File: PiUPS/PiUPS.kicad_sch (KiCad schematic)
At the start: 101 parts, among them J1 USB_C_Receptacle_USB2.0, J2 Raspberry_Pi_2_3, J3 USB_A, J4 USB_B_Micro, J5 Screw_Terminal_01x02, J6 Screw_Terminal_01x02, Q1 IRF7404, Q2 IRF7404, Q3 IRLML2803TRPBF, Q4 IRF7404, Q5 IRF7404, Q6 IRLML2803TRPBF, Q7 IRLML2803TRPBF, SW1 MODE (JS102011SAQN), SW2 SW_MEC_5E, U1 LM393, U2 BQ25601, U3 TPS61088RHLR, U4 DS3231M

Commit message: minor improvements and cleanup
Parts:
- removed R17: USR, Resistor_SMD:R_0805_2012Metric_Pad1.20x1.40mm_HandSolder, symbol Device:R
- added R?: 470, Resistor_SMD:R_0805_2012Metric_Pad1.20x1.40mm_HandSolder, symbol Device:R
- R?: value 100 -> 470
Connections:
- net +BATT: now also SW2.1, SW2.2
- net GND: no longer SW2.1, SW2.2
- net at SW2.3 (K), SW2.4 (A): now also R?.2; no longer U2.12 (~{QON})
- net at Q?.1, R?.1, R?.2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: now also R?.1
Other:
- note added: "100 works"
- note added: "Enable without input voltage"
- note added: "Raplce with bq25895"
- note removed: "Probably can be lowered to 470"
- moved on the sheet: D4, D?, SW2, U1C

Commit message: assigned footprints
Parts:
- removed C1: 47nF, Capacitor_SMD:C_0805_2012Metric_Pad1.18x1.45mm_HandSolder, symbol Device:C
- removed C15, C18: 10uF, Capacitor_SMD:C_1206_3216Metric_Pad1.33x1.80mm_HandSolder, symbol Device:C
- removed D2: LED_G, LED_SMD:LED_0805_2012Metric, symbol Device:LED
- removed R28, R31, R33: 10k, Resistor_SMD:R_0805_2012Metric_Pad1.20x1.40mm_HandSolder, symbol Device:R
- removed U2: BQ25601, Package_DFN_QFN:Texas_S-PWQFN-N24_EP2.7x2.7mm_ThermalVias, symbol Battery_Management:BQ25601
- added C10, C6: 10uF, Capacitor_SMD:C_1206_3216Metric_Pad1.33x1.80mm_HandSolder, symbol Device:C
- added C12: 100nF, Capacitor_SMD:C_0805_2012Metric_Pad1.18x1.45mm_HandSolder, symbol Device:C
- added C5: 47nF, Capacitor_SMD:C_0805_2012Metric_Pad1.18x1.45mm_HandSolder, symbol Device:C
- added D3, D4: 1PS76SB40.115, Diode_SMD:D_SOD-323_HandSoldering, symbol Diode:1N4007
- added R1, R17: 10k, Resistor_SMD:R_0805_2012Metric_Pad1.20x1.40mm_HandSolder, symbol Device:R
- added R11, R12, R24, R27: 470, Resistor_SMD:R_0805_2012Metric_Pad1.20x1.40mm_HandSolder, symbol Device:R
- added R19: 1k, Resistor_SMD:R_0805_2012Metric_Pad1.20x1.40mm_HandSolder, symbol Device:R
- added R23: 100, Resistor_SMD:R_0805_2012Metric_Pad1.20x1.40mm_HandSolder, symbol Device:R
- added RT1: 10k, Resistor_SMD:R_0603_1608Metric, symbol Device:R
- added U2: BQ25895RTW, Package_DFN_QFN:Texas_S-PWQFN-N24_EP2.7x2.7mm_ThermalVias, symbol Battery_Management:BQ25895RTW
- added U4: DW01, Package_TO_SOT_SMD:SOT-23-6, symbol dw01:DW01
- added U5: FS8205A, Package_SO:TSSOP-8_4.4x3mm_P0.65mm, symbol fs8205a:FS8205A
- C20: renamed from C21; value 220uF -> 1000uF
- D1: renamed from D?; value 1N4007 -> 1PS76SB40.115; footprint Diode_THT:D_DO-41_SOD81_P10.16mm_Horizontal -> Diode_SMD:D_SOD-323_HandSoldering
- D2: renamed from D3; footprint LED_SMD:LED_0805_2012Metric -> LED_SMD:LED_1206_3216Metric_Pad1.42x1.75mm_HandSolder
- D6: renamed from D4; value 1N4001 -> 1PS76SB40.115; footprint Diode_SMD:D_1206_3216Metric_Pad1.42x1.75mm_HandSolder -> Diode_SMD:D_SOD-323_HandSoldering
- J2: renamed from J4; footprint Connector_USB:USB_Micro-B_GCT_USB3076-30-A -> Connector_USB:USB_Micro-B_Amphenol_10103594-0001LF_Horizontal
- J4: renamed from J3; footprint Connector_USB:USB_A_Stewart_SS-52100-001_Horizontal -> USB:SAMTEC_USB-A-S-X-X-SM2
- R13: value 5.1k -> 10k
- gave numbers to parts that had none: 11
- renumbered C9 to C1, C16 to C11, C5 to C13, C12 to C14, C6 to C15, C14 to C16, C7 to C17, C17 to C18, C13 to C19, C4 to C2, C22 to C21, C23 to C22, C24 to C23, C25 to C24, C20 to C26, C10 to C3, C11 to C4, C19 to C7, C2 to C8, C3 to C9, D1 to D5, J6 to J3, J2 to J6, L2 to L1, L1 to L2, Q7 to Q3, Q1 to Q4, Q3 to Q5, Q4 to Q6, Q6 to Q7, Q2 to Q8, Q5 to Q9, R9 to R10, R25 to R16, R1 to R20, R5 to R21, R27 to R22, R24 to R25, R7 to R26, R20 to R28, R3 to R29, R16 to R30, R26 to R31, R2 to R32, R19 to R33, R21 to R34, R38 to R36, R39 to R37, R36 to R38, R4 to R39, R37 to R40, R23 to R41, R6 to R42, R12 to R43, R30 to R44, R14 to R45, R35 to R46, R10 to R47, R8 to R48, R34 to R49, R32 to R6, R11 to R7, R15 to R9, SW2 to SW1, SW1 to SW2, U4 to U6
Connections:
- net +5V: now also R24.2, U2.1 (VBUS)
- net +BATT: now also R23.1, U2.13 (BAT), U2.14 (BAT)
- net 2V4: now also R27.1
- net GND: now also C12.2, R1.1, U4.6 (GND), U5.2 (S1), U5.3 (S1); no longer C8.2, C9.2, R18.2
- net INT: now also U2.7 (INT)
- net SCL: now also U2.5 (SCL)
- net SDA: now also U2.6 (SDA)
- net VOUT: now also R26.2, R35.2, U1.8 (V+), R27.2; no longer SW2.2 (B)
- net VSYS: now also R9.1, U2.15 (SYS), U2.16 (SYS); no longer D2.2 (A)
- net at L2.1: now also C5.1, U2.19 (SW), U2.20 (SW)
- net at R9.2: now also D2.2 (A)
- net at R13.2: now also U2.9 (~{CE})
- net GND1: now reaches R18.1
- net GND1: now also C8.2, C9.2, R13.1, C10.2, C6.1, R12.2, R19.1, RT1.1, U2.17 (PGND), U2.18 (PGND), U2.25 (PGND), U2.8 (OTG), U5.6 (S2), U5.7 (S2)
- net at D2.1 (K): now also U2.4 (STAT); no longer R9.1
- net at SW2.3 (C): now also R1.2
- net at R2.1, R3.2, R4.2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: now also SW2.1 (A); no longer Q1.1
- new net: Q1.1, SW2.2 (B)
- new net: D4.1 (K), U4.1 (OD), U5.4 (G1)
- new net: R19.2, U4.2 (CS)
- new net: D3.1 (K), U4.3 (OC), U5.5 (G2)
- new net: C12.1, R23.2, U4.5 (VCC)
- new net: D3.2 (A), D4.2 (A), R24.1
- new net: C5.2, U2.21 (BTST)
- new net: R11.1, U2.10 (ILIM)
- new net: R17.1, R18.2, RT1.2, U2.11 (TS)
- new net: U2.2 (D+), U2.3 (D-)
- new net: C6.2, R17.2, U2.22 (REGN)
- new net: C10.1, U2.23 (PMID)
- new net: R11.2, R12.1
- no-connect marks 36 -> 41
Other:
- note added: "B57351V5103H060"
- note added: "Calculate later"
- note removed: "Raplce with bq25895"
- note removed: "TODO Edit the shematic to the new version"
- note removed: "add dw01 between bat and BQ IC"
- moved on the sheet: BT1, C1, C11, C13, C14, C15, C16, C17, C18, C19, C20, C21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

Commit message: beginning of routing
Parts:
- L2: footprint Inductor_SMD:L_10.4x10.4_H4.8 -> Inductor_SMD:L_6.3x6.3_H3
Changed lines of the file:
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@@
     (property "Reference" "L2" (id 0) (at 125.095 46.99 90))
     (property "Value" "1uH" (id 1) (at 125.095 48.895 90))
-    (property "Footprint" "Inductor_SMD:L_10.4x10.4_H4.8" (id 2) (at 125.095 50.8 0)
+    (property "Footprint" "Inductor_SMD:L_6.3x6.3_H3" (id 2) (at 125.095 50.8 0)
       (effects (font (size 1.27 1.27)) hide)
     )
@@
     )
     (path "/00000000-0000-0000-0000-0000610e819d"
-      (reference "L2") (unit 1) (value "1uH") (footprint "Inductor_SMD:L_10.4x10.4_H4.8")
+      (reference "L2") (unit 1) (value "1uH") (footprint "Inductor_SMD:L_6.3x6.3_H3")
     )
     (path "/00000000-0000-0000-0000-0000617428a3"

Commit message: Continued routing
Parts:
- removed C8: 10uF, Capacitor_SMD:C_1206_3216Metric_Pad1.33x1.80mm_HandSolder, symbol Device:C
- renumbered C2 to C1, C15 to C10, C17 to C11, C20 to C12, C21 to C13, C22 to C14, C23 to C15, C24 to C16, C25 to C17, C1 to C18, C3 to C19, C5 to C2, C4 to C20, C14 to C21, C16 to C22, C11 to C23, C18 to C24, C7 to C25, C9 to C3, C10 to C4, C12 to C5, C19 to C6, C6 to C7, C26 to C8, C13 to C9, D5 to D1, D3 to D2, D4 to D3, D2 to D4, D1 to D5, J6 to J4, J4 to J5, J5 to J6, L2 to L1, L1 to L2, Q4 to Q1, Q8 to Q2, Q5 to Q3, Q6 to Q4, Q9 to Q5, Q7 to Q6, Q3 to Q7, Q2 to Q8, Q1 to Q9, R32 to R1, R45 to R10, R23 to R11, R41 to R13, R17 to R14, R19 to R15, R24 to R16, R9 to R17, R13 to R18, R18 to R19, R29 to R2, R44 to R20, R6 to R21, R49 to R22, R46 to R23, R38 to R24, R40 to R25, R20 to R26, R36 to R27, R21 to R28, R37 to R29, R26 to R3, R5 to R30, R1 to R31, R25 to R32, R16 to R33, R22 to R34, R2 to R35, R3 to R36, R8 to R37, R4 to R38, R14 to R39, R27 to R4, R39 to R40, R15 to R41, R47 to R43, R43 to R44, R30 to R45, R33 to R46, R28 to R47, R34 to R48, R31 to R49, R48 to R5, R10 to R6, R35 to R8, R11 to R9, U4 to U3, U5 to U4, U3 to U5

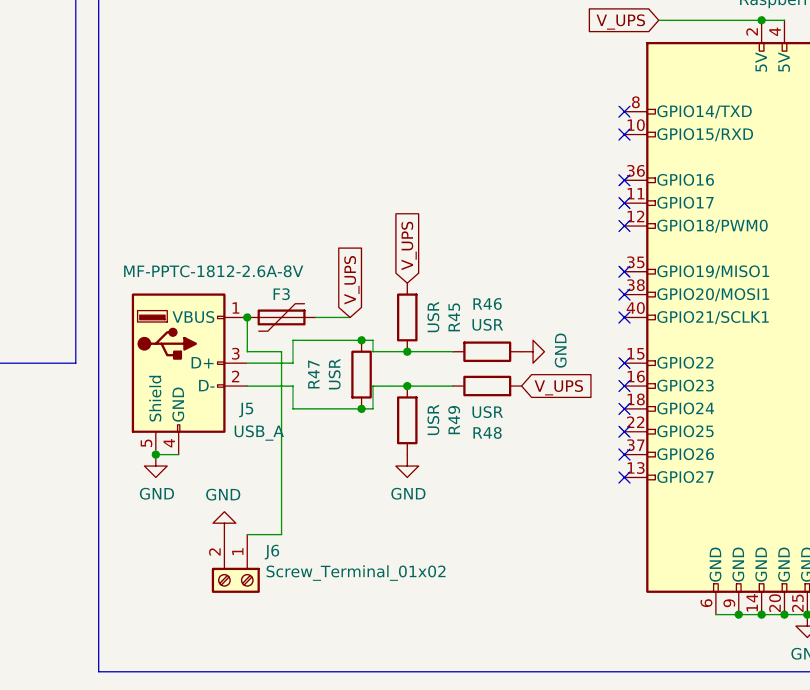
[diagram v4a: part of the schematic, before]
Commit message: almost finished routing
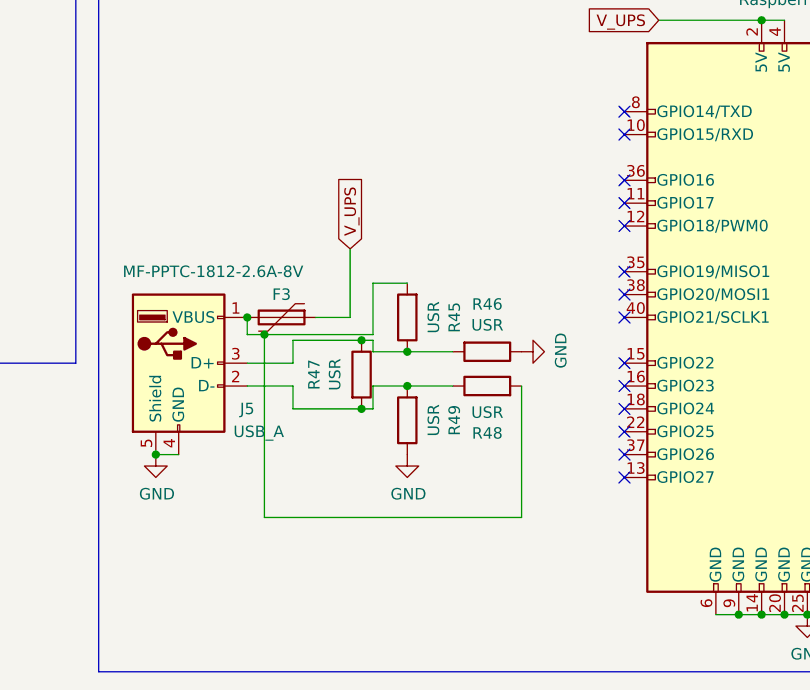
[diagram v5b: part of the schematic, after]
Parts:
- removed J6: Screw_Terminal_01x02, TerminalBlock:TerminalBlock_Altech_AK300-2_P5.00mm, symbol Connector:Screw_Terminal_01x02
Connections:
- net V_UPS: no longer R45.2, R48.2
- net at F3.2, J5.1 (VBUS): now also R45.2, R48.2
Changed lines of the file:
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@@
   (junction (at 48.26 106.68) (diameter 0) (color 0 0 0 0)
   )
+  (junction (at 235.585 210.185) (diameter 0) (color 0 0 0 0)
+  )
   (junction (at 337.82 57.15) (diameter 0) (color 0 0 0 0)
   )
@@
   (no_connect (at 275.59 195.58))
   (no_connect (at 113.665 73.66))
+  (wire (pts (xy 247.65 204.47) (xy 247.65 210.185))
+    (stroke (width 0) (type default) (color 0 0 0 0))
+  )
   (wire (pts (xy 363.22 101.6) (xy 363.22 49.53))
     (stroke (width 0) (type default) (color 0 0 0 0))
@@
     (stroke (width 0) (type default) (color 0 0 0 0))
   )
-  (wire (pts (xy 233.68 208.28) (xy 233.68 212.09))
+  (wire (pts (xy 233.68 208.28) (xy 233.68 210.185))
     (stroke (width 0) (type default) (color 0 0 0 0))
   )
@@
     (stroke (width 0) (type default) (color 0 0 0 0))
   )
+  (wire (pts (xy 245.11 200.66) (xy 245.11 208.28))
+    (stroke (width 0) (type default) (color 0 0 0 0))
+  )
   (wire (pts (xy 46.355 162.56) (xy 51.435 162.56))
     (stroke (width 0) (type default) (color 0 0 0 0))
@@
     (stroke (width 0) (type default) (color 0 0 0 0))
   )
-  (wire (pts (xy 237.49 232.41) (xy 233.68 232.41))
-    (stroke (width 0) (type default) (color 0 0 0 0))
-  )
   (wire (pts (xy 255.27 71.12) (xy 255.27 48.26))
     (stroke (width 0) (type default) (color 0 0 0 0))
@@
     (stroke (width 0) (type default) (color 0 0 0 0))
   )
+  (wire (pts (xy 264.16 215.9) (xy 264.16 230.505))
+    (stroke (width 0) (type default) (color 0 0 0 0))
+  )
   (polyline (pts (xy 30.48 213.36) (xy 214.63 213.36))
     (stroke (width 0) (type default) (color 0 0 0 0))
@@
     (stroke (width 0) (type default) (color 0 0 0 0))
   )
+  (wire (pts (xy 264.16 230.505) (xy 235.585 230.505))
+    (stroke (width 0) (type default) (color 0 0 0 0))
+  )
   (wire (pts (xy 83.185 175.26) (xy 83.185 144.78))
     (stroke (width 0) (type default) (color 0 0 0 0))
@@
     (stroke (width 0) (type default) (color 0 0 0 0))
   )
+  (wire (pts (xy 247.65 210.185) (xy 235.585 210.185))
+    (stroke (width 0) (type default) (color 0 0 0 0))
+  )
   (wire (pts (xy 317.5 127) (xy 316.23 127))
     (stroke (width 0) (type default) (color 0 0 0 0))
@@
     (stroke (width 0) (type default) (color 0 0 0 0))
   )
+  (wire (pts (xy 235.585 210.185) (xy 233.68 210.185))
+    (stroke (width 0) (type default) (color 0 0 0 0))
+  )
   (wire (pts (xy 76.835 144.78) (xy 83.185 144.78))
     (stroke (width 0) (type default) (color 0 0 0 0))
@@
     (stroke (width 0) (type default) (color 0 0 0 0))
   )
-  (wire (pts (xy 233.68 212.09) (xy 237.49 212.09))
-    (stroke (width 0) (type default) (color 0 0 0 0))
-  )
   (wire (pts (xy 85.09 63.5) (xy 93.345 63.5))
     (stroke (width 0) (type default) (color 0 0 0 0))
@@
     (stroke (width 0) (type default) (color 0 0 0 0))
   )
+  (wire (pts (xy 251.46 204.47) (xy 247.65 204.47))
+    (stroke (width 0) (type default) (color 0 0 0 0))
+  )
   (wire (pts (xy 147.32 87.63) (xy 147.32 85.09))
     (stroke (width 0) (type default) (color 0 0 0 0))
@@
     (stroke (width 0) (type default) (color 0 0 0 0))
   )
-  (wire (pts (xy 237.49 212.09) (xy 237.49 232.41))
-    (stroke (width 0) (type default) (color 0 0 0 0))
-  )
   (wire (pts (xy 298.45 71.12) (xy 255.27 71.12))
     (stroke (width 0) (type default) (color 0 0 0 0))
@@
     (stroke (width 0) (type default) (color 0 0 0 0))
   )
+  (wire (pts (xy 235.585 230.505) (xy 235.585 210.185))
+    (stroke (width 0) (type default) (color 0 0 0 0))
+  )
   (wire (pts (xy 117.475 182.88) (xy 117.475 187.96))
     (stroke (width 0) (type default) (color 0 0 0 0))
@@
     )
   )
-  (global_label "V_UPS" (shape input) (at 264.16 215.9 0) (fields_autoplaced)
-    (effects (font (size 1.27 1.27)) (justify left))
-    (property "Intersheet References" "${INTERSHEET_REFS}" (id 0) (at 40.64 0 0)
-      (effects (font (size 1.27 1.27)) hide)
-    )
-  )
   (global_label "SDA" (shape input) (at 321.31 193.04 0) (fields_autoplaced)
     (effects (font (size 1.27 1.27)) (justify left))
@@
     )
   )
-  (global_label "V_UPS" (shape input) (at 245.11 208.28 90) (fields_autoplaced)
+  (global_label "V_UPS" (shape input) (at 245.11 200.66 90) (fields_autoplaced)
     (effects (font (size 1.27 1.27)) (justify left))
-    (property "Intersheet References" "${INTERSHEET_REFS}" (id 0) (at 40.64 0 0)
+    (property "Intersheet References" "${INTERSHEET_REFS}" (id 0) (at 40.64 -7.62 0)
       (effects (font (size 1.27 1.27)) hide)
     )
@@
     )
   )
-  (global_label "V_UPS" (shape input) (at 251.46 204.47 90) (fields_autoplaced)
-    (effects (font (size 1.27 1.27)) (justify left))
-    (property "Intersheet References" "${INTERSHEET_REFS}" (id 0) (at 40.64 0 0)
-      (effects (font (size 1.27 1.27)) hide)
-    )
-  )
   (global_label "2V4" (shape input) (at 81.915 182.88 0) (fields_autoplaced)
     (effects (font (size 1.27 1.27)) (justify left))
@@
     (pin "8")
   )
-  (symbol (lib_id "Connector:Screw_Terminal_01x02") (at 233.68 237.49 270) (unit 1)
-    (in_bom yes) (on_board yes)
-    (property "Reference" "J6" (id 0) (at 235.712 234.2388 90)
-      (effects (font (size 1.27 1.27)) (justify left))
-    )
-    (property "Value" "Screw_Terminal_01x02" (id 1) (at 235.712 236.5502 90)
-      (effects (font (size 1.27 1.27)) (justify left))
-    )
-    (property "Footprint" "TerminalBlock:TerminalBlock_Altech_AK300-2_P5.00mm" (id 2) (at 233.68 237.49 0)
-      (effects (font (size 1.27 1.27)) hide)
-    )
-    (property "Datasheet" "~" (id 3) (at 233.68 237.49 0)
-      (effects (font (size 1.27 1.27)) hide)
-    )
-    (pin "1")
-    (pin "2")
-  )
-  (symbol (lib_id "power:GND") (at 231.14 232.41 180) (unit 1)
-    (in_bom yes) (on_board yes)
-    (property "Reference" "#PWR040" (id 0) (at 231.14 226.06 0)
-      (effects (font (size 1.27 1.27)) hide)
-    )
-    (property "Value" "GND" (id 1) (at 231.013 228.0158 0))
-    (property "Footprint" "" (id 2) (at 231.14 232.41 0)
-      (effects (font (size 1.27 1.27)) hide)
-    )
-    (property "Datasheet" "" (id 3) (at 231.14 232.41 0)
-      (effects (font (size 1.27 1.27)) hide)
-    )
-    (pin "1")
-  )
   (symbol (lib_id "Connector:USB_B_Micro") (at 50.8 96.52 0) (unit 1)
     (in_bom yes) (on_board yes)
@@
       (reference "#PWR039") (unit 1) (value "GND") (footprint "")
     )
-    (path "/00000000-0000-0000-0000-00006140b341"
-      (reference "#PWR040") (unit 1) (value "GND") (footprint "")
-    )
     (path "/00000000-0000-0000-0000-0000616d14e8"
       (reference "#PWR041") (unit 1) (value "GND") (footprint "")
@@
       (reference "J5") (unit 1) (value "USB_A") (footprint "USB:SAMTEC_USB-A-S-X-X-SM2")
     )
-    (path "/00000000-0000-0000-0000-000061403373"
-      (reference "J6") (unit 1) (value "Screw_Terminal_01x02") (footprint "TerminalBlock:TerminalBlock_Altech_AK300-2_P5.00mm")
-    )
     (path "/00000000-0000-0000-0000-0000610e819d"

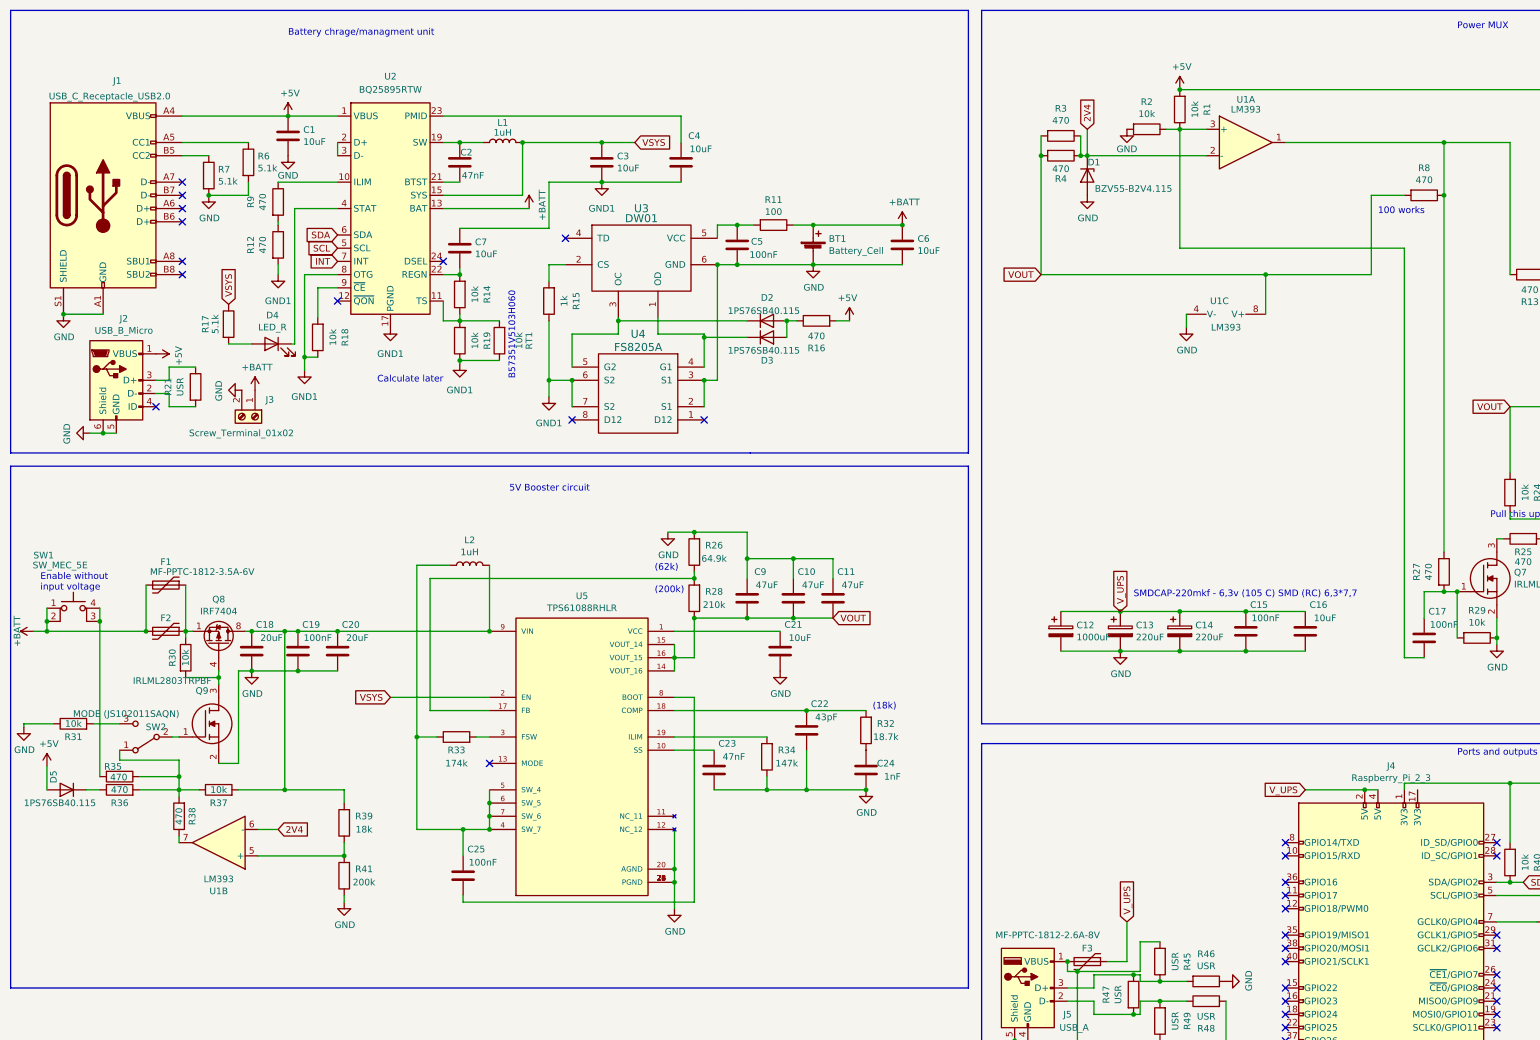
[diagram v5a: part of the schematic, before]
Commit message: updated development schematic
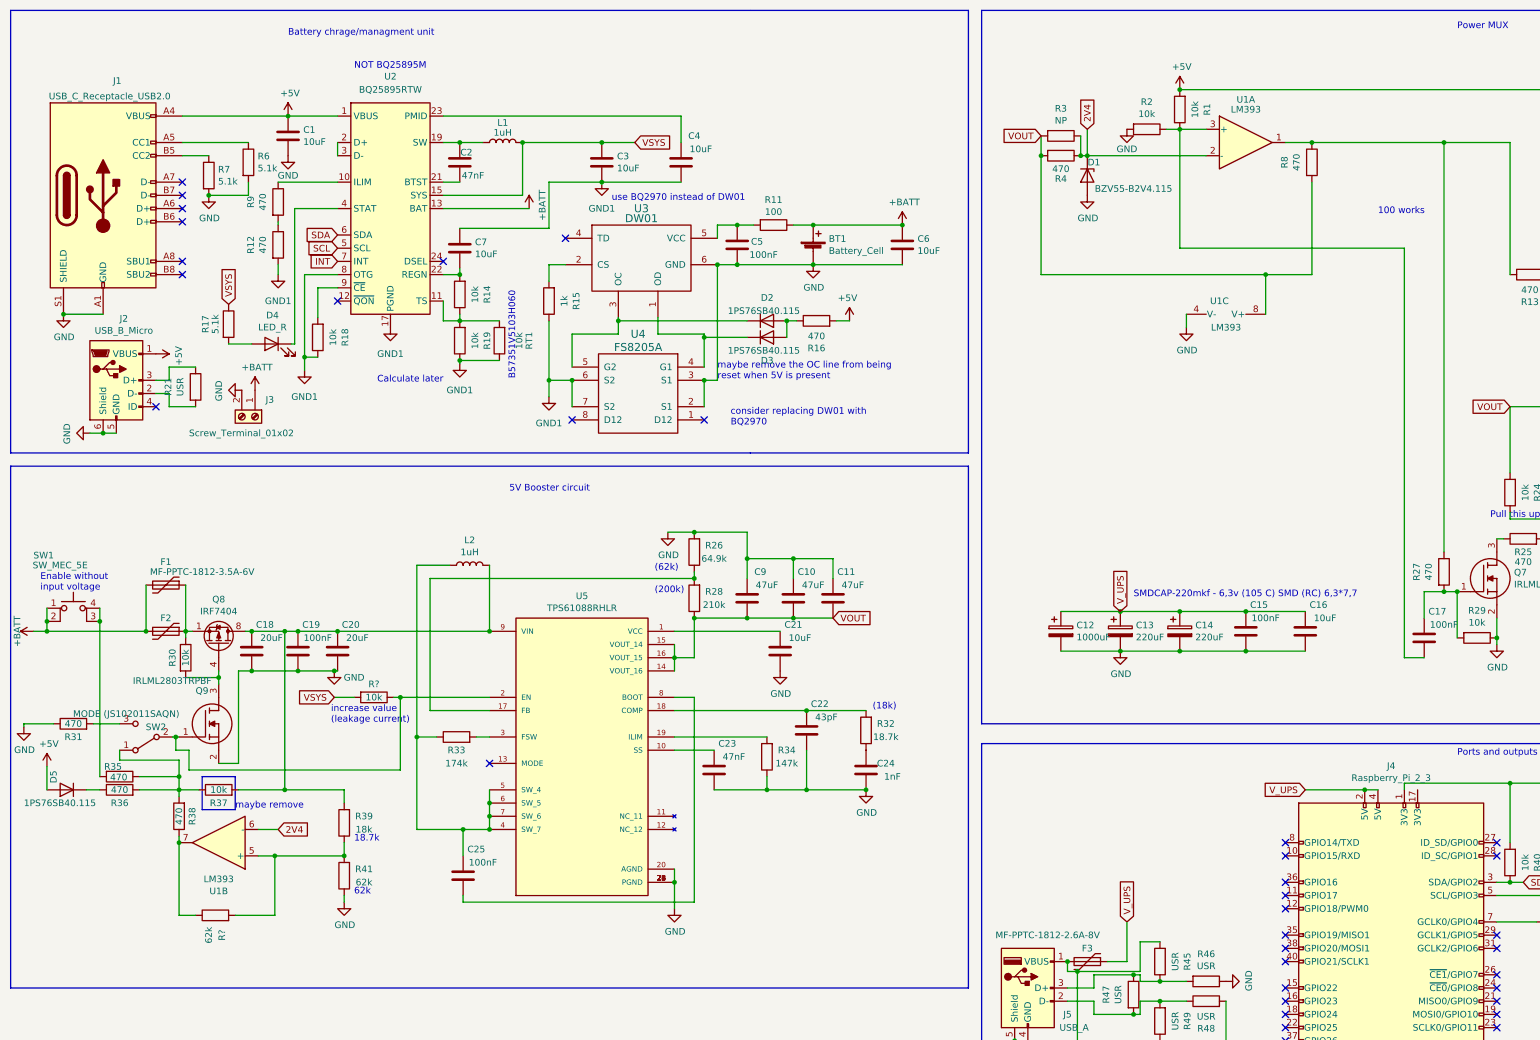
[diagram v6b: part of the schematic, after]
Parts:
- added R?: 62k, Resistor_SMD:R_0805_2012Metric_Pad1.20x1.40mm_HandSolder, symbol Device:R
- added R?: 10k, Resistor_SMD:R_0805_2012Metric_Pad1.20x1.40mm_HandSolder, symbol Device:R
- R3: value 470 -> NP
- R31: value 10k -> 470
- R41: value 200k -> 62k
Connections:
- net GND: no longer U5.12 (NC_12)
- net VSYS: now also R?.2; no longer U5.2 (EN)
- net at Q9.1, SW2.2 (B): now also U5.2 (EN), R?.1
- net at R39.1, R41.2, U1.5 (+): now also R?.2
- net at R38.1, U1.7: now also R?.1
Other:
- note added: "18.7k"
- note added: "62k"
- note added: "NOT BQ25895M"
- note added: "consider replacing DW01 with BQ2970"
- note added: "increase value (leakage current)"
- note added: "maybe remove"
- note added: "maybe remove the OC line from being reset when 5V is present"
- note added: "use BQ2970 instead of DW01"
- moved on the sheet: R8
